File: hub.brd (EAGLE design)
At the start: 64.1 x 51.7 mm, 50 parts, among them U1 LM3526-L, X1 12MHz

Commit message: complete BOM
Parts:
- LB1, LB6: value (none) -> 220
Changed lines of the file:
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@@
 <element name="C14" library="rcl" library_urn="urn:adsk.eagle:library:334" package="C0805" package3d_urn="urn:adsk.eagle:package:23617/2" value="18P" x="35.943" y="33.982">
 <attribute name="DIGIKEY" value="1276-1089-1-ND" x="35.943" y="33.982" size="1.778" layer="27" display="off"/>
+<attribute name="MPN" value="CL10C180JB8NNNC" x="35.943" y="33.982" size="1.778" layer="27" display="off"/>
 <attribute name="OC_MOUSER" value="77-VJ0603A180JXACBC" x="35.943" y="33.982" size="1.778" layer="27" display="off"/>
 </element>
 <element name="C15" library="rcl" library_urn="urn:adsk.eagle:library:334" package="C0805" package3d_urn="urn:adsk.eagle:package:23617/2" value="18P" x="35.2" y="36.6">
 <attribute name="DIGIKEY" value="1276-1089-1-ND" x="35.2" y="36.6" size="1.778" layer="27" display="off"/>
+<attribute name="MPN" value="CL10C180JB8NNNC" x="35.2" y="36.6" size="1.778" layer="27" display="off"/>
 <attribute name="OC_MOUSER" value="77-VJ0603A180JXACBC" x="35.2" y="36.6" size="1.778" layer="27" display="off"/>
 </element>
@@
 <attribute name="OC_MOUSER" value="595-SN65220DBVR" x="47.9" y="19.9" size="1.778" layer="27" rot="R270" display="off"/>
 </element>
-<element name="LB1" library="rcl" library_urn="urn:adsk.eagle:library:334" package="R0805" package3d_urn="urn:adsk.eagle:package:23553/2" value="" x="47.5" y="16.9" rot="R180"/>
+<element name="LB1" library="rcl" library_urn="urn:adsk.eagle:library:334" package="R0805" package3d_urn="urn:adsk.eagle:package:23553/2" value="220" x="47.5" y="16.9" rot="R180">
+<attribute name="DIGIKEY" value="490-1054-1-ND" x="47.5" y="16.9" size="1.778" layer="27" rot="R180" display="off"/>
+<attribute name="MPN" value="BLM21PG221SN1D" x="47.5" y="16.9" size="1.778" layer="27" rot="R180" display="off"/>
+<attribute name="OC_MOUSER" value="81-BLM21P221SG" x="47.5" y="16.9" size="1.778" layer="27" rot="R180" display="off"/>
+</element>
 <element name="C12" library="rcl" library_urn="urn:adsk.eagle:library:334" package="C0805" package3d_urn="urn:adsk.eagle:package:23617/2" value="0.1uF" x="28.064" y="21.504" rot="MR0">
 <attribute name="DIGIKEY" value="490-1666-1-ND" x="28.064" y="21.504" size="1.778" layer="28" rot="MR0" display="off"/>
@@
 <attribute name="OC_MOUSER" value="81-GRM40X104K50L" x="28.064" y="21.504" size="1.778" layer="28" rot="MR0" display="off"/>
 </element>
-<element name="LB6" library="rcl" library_urn="urn:adsk.eagle:library:334" package="R0805" package3d_urn="urn:adsk.eagle:package:23553/2" value="" x="31.006" y="37.026" rot="MR180"/>
+<element name="LB6" library="rcl" library_urn="urn:adsk.eagle:library:334" package="R0805" package3d_urn="urn:adsk.eagle:package:23553/2" value="220" x="31.006" y="37.026" rot="MR180">
+<attribute name="DIGIKEY" value="490-1054-1-ND" x="31.006" y="37.026" size="1.778" layer="28" rot="MR180" display="off"/>
+<attribute name="MPN" value="BLM21PG221SN1D" x="31.006" y="37.026" size="1.778" layer="28" rot="MR180" display="off"/>
+<attribute name="OC_MOUSER" value="81-BLM21P221SG" x="31.006" y="37.026" size="1.778" layer="28" rot="MR180" display="off"/>
+</element>
 <element name="J3" library="InputOutputIO (rev17e)" package="61400826021" value="" x="9.9" y="10.5">
 <attribute name="DIGIKEY" value="732-2107-ND" x="9.9" y="10.5" size="1.778" layer="27" display="off"/>

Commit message: finish pin-strapping
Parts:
- added R5, R6: 10K, rcl:M0805
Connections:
- removed net NOVRP3: U$1.30
- removed net NOVRP4: U$1.28
- new net N$6: R6.2, U$1.23
- new net N$7: R5.2, U$1.32
- net +3V3: now also R5.1, R6.1, U$1.28, U$1.30

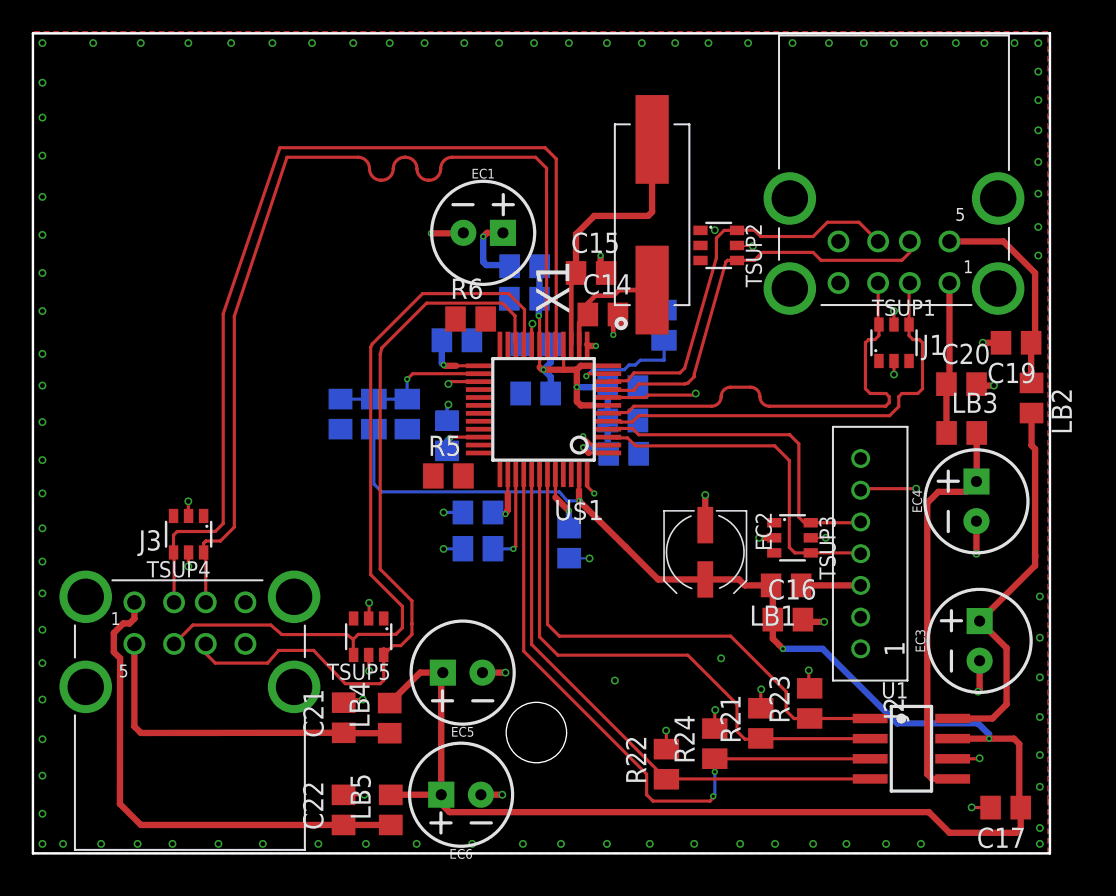
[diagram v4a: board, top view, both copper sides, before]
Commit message: re-route USB for oshpark PCBs
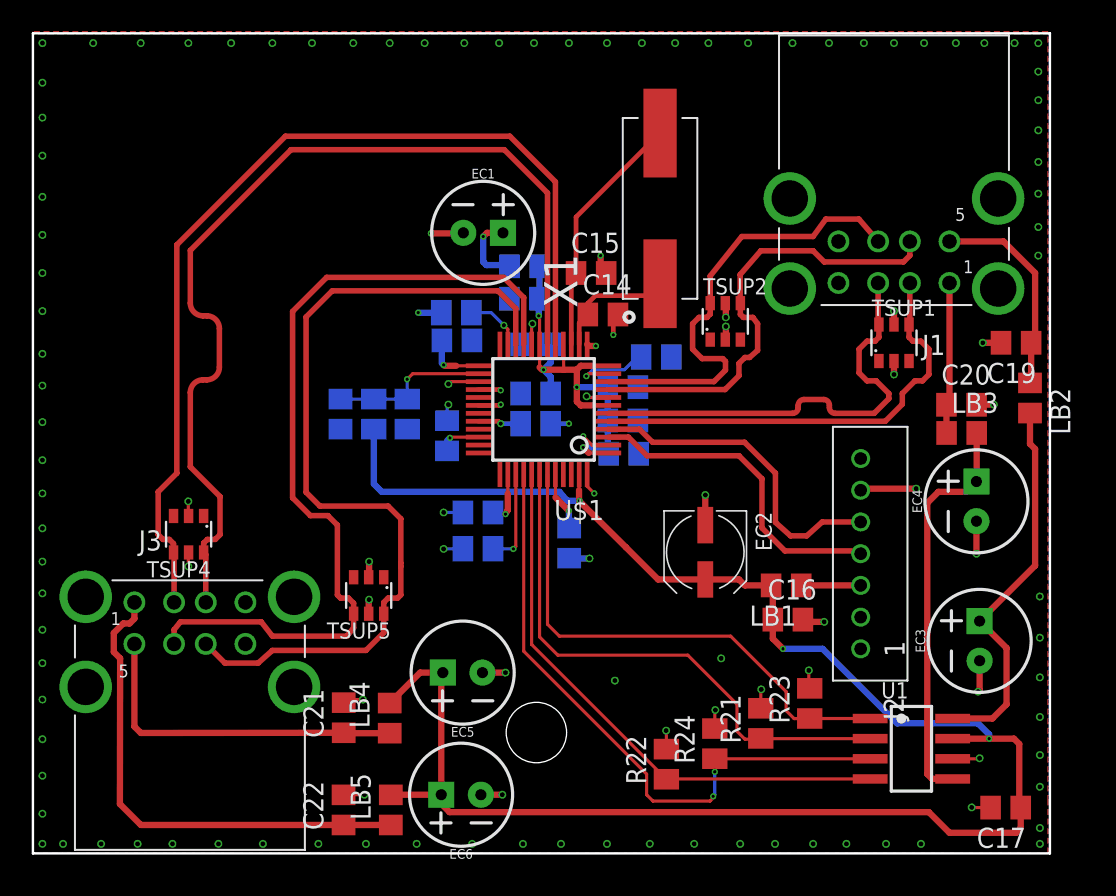
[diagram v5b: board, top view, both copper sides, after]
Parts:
- removed TSUP3: SN65220DBV, sn65220_40:SOT23-6
- moved R5 6.41 mm to (31.7, 27.1), flipped to the bottom
- moved TSUP2 4.81 mm to (43.7, 33.5), turned to 0 degrees
- moved TSUP5 2.60 mm to (21.2, 16.3)
- moved R3 2.06 mm to (39.3, 31.3), turned to 0 degrees
- moved C20 1.30 mm to (58.6, 28.3)
- moved R6 0.98 mm to (26.7, 34.1), flipped to the bottom, turned to 180 degrees
- moved X1 0.64 mm to (39.5, 40.7)
- moved LB2 0.10 mm to (62.9, 28.7)
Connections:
- net D0_N: no longer TSUP3.4
- net D0_P: no longer TSUP3.6
- net GND: no longer TSUP3.2, TSUP3.5
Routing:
- net D4_P: track 48.4 -> 54.8 mm
- net D4_N: track 48.8 -> 54.6 mm
- net GND: track 50.7 -> 45.2 mm, vias 123 -> 121
- net +3V3: track 24.4 -> 29.9 mm, vias 10 -> 14
- net N$6: track 0.00 -> 3.68 mm, vias 0 -> 1
- net D2_P: track 25.8 -> 29.0 mm
- net D2_N: track 26.4 -> 29.2 mm
- net N$7: track 0.00 -> 2.71 mm, vias 0 -> 1
- net RREF: track 8.04 -> 5.43 mm
- net D0_N: track 22.6 -> 20.8 mm
- net XOUT: track 17.0 -> 15.6 mm
- net D3_P: track 60.2 -> 61.4 mm
- net D0_P: track 21.6 -> 20.8 mm
- net XIN: track 7.22 -> 7.88 mm

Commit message: finish silk screen
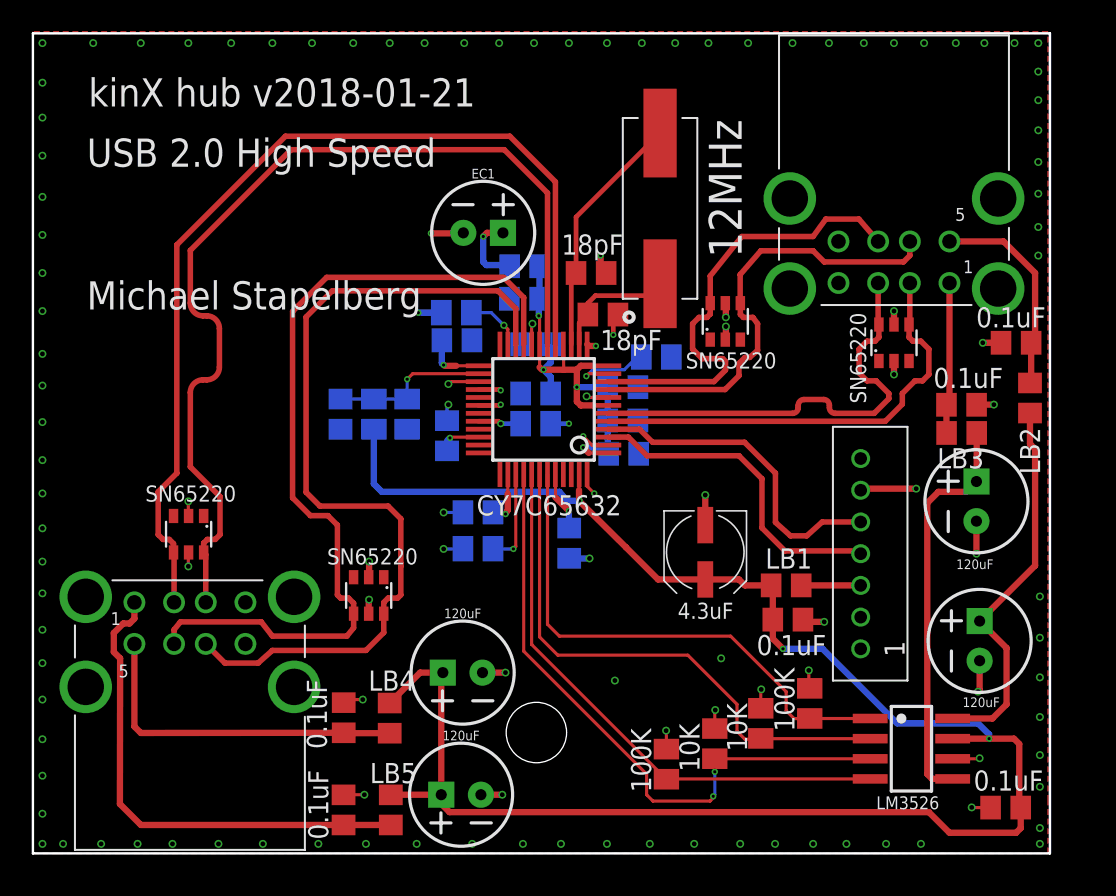
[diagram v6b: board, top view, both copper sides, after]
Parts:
- C14, C15: value 18P -> 18pF
- TSUP1, TSUP2, TSUP4, TSUP5: value SN65220DBV -> SN65220
- U$1: value CY7C65634-48AXCT -> CY7C65632
- U1: value LM3526-L -> LM3526
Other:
- board text added: "Michael Stapelberg"
- board text added: "USB 2.0 High Speed"
- board text added: "kinX hub v2018-01-21"
